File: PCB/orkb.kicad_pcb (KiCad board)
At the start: 2 copper layers, 148.5 x 113.3 mm, 109 parts, among them J1 USB_C_Receptacle_USB2.0, P1 OLED, SW1 MXHS, SW10 MXHS, SW11 MXHS, SW12 MXHS, SW13 MXHS, SW14 MXHS, SW15 MXHS, SW16 MXHS, SW17 MXHS, SW18 MXHS, SW19 MXHS, SW2 MXHS, SW20 MXHS, SW21 MXHS, SW22 MXHS, SW23 MXHS, SW24 MSK12C02, SW25 MSK12C02, SW3 MXHS, SW4 MXHS, SW5 MXHS, SW6 MXHS, SW7 MXHS, SW8 MXHS, SW9 MXHS, U1 ProMicro, U2 SRV05-4, U3 SRV05-4

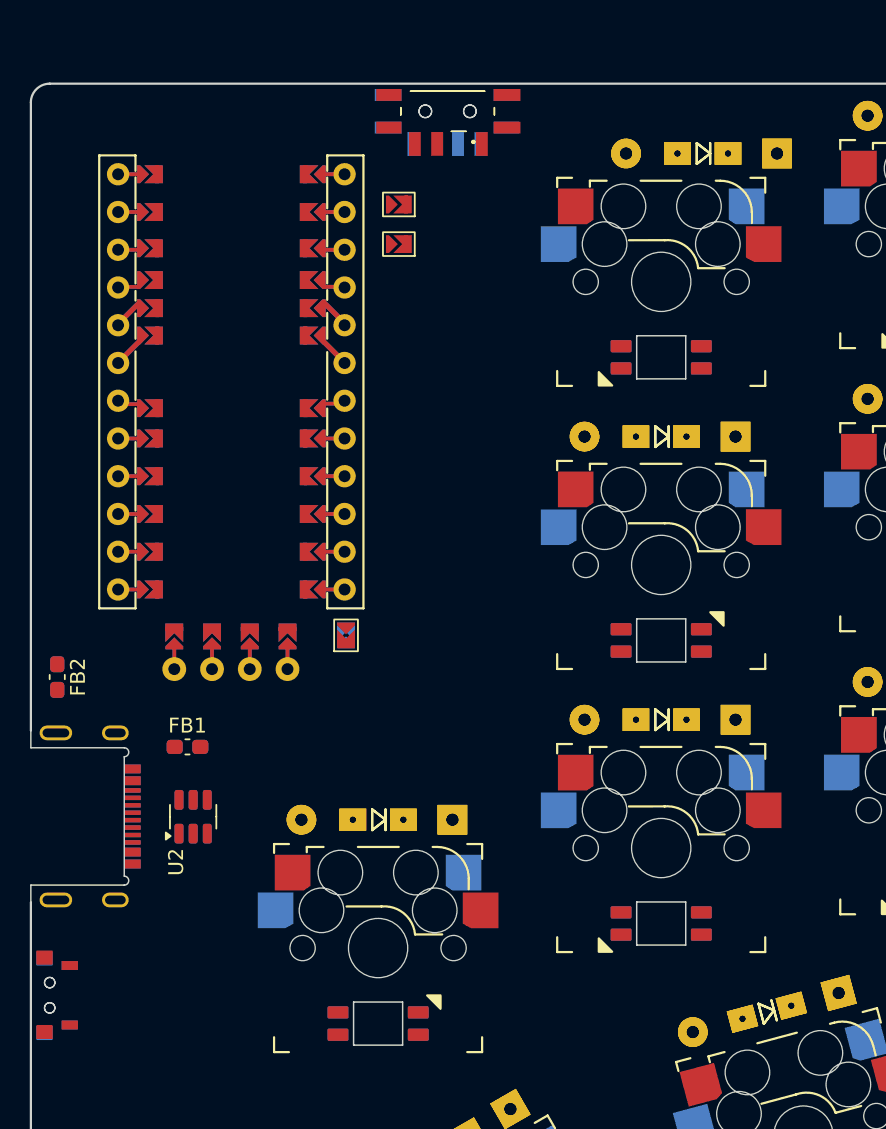
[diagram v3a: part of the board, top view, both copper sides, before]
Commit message: Added underglow LED to schematic
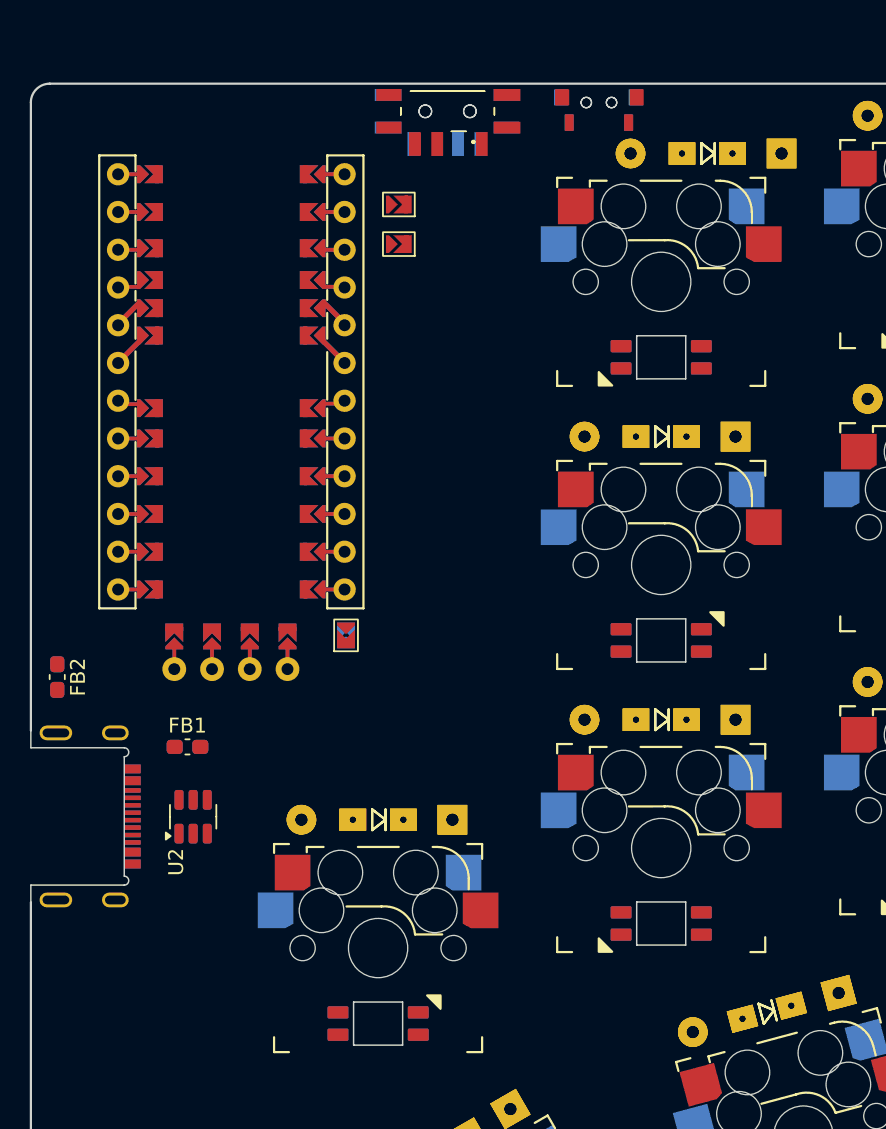
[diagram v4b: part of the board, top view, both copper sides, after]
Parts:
- moved RES1 70.5 mm to (103.5, 48.5), turned to 0 degrees
- moved RES2 70.5 mm to (103.5, 48.5), turned to 180 degrees
- moved D1 0.30 mm to (110.8, 51.9)
- moved D23 0.30 mm to (110.8, 51.9)
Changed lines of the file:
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@@
 		(placed yes)
 		(layer "F.Cu")
-		(at 110.49 51.943 180)
+		(at 110.793 51.943 180)
 		(descr "Diode, DO-41, SOD81, Horizontal, RM 10mm,")
 		(tags "Diode, DO-41, SOD81, Horizontal, RM 10mm, 1N4007, SB140,")
@@
 	(footprint "SplitKeyboard_Common:YTS-A002"
 		(layer "F.Cu")
-		(at 66.548 108.585 90)
+		(at 103.505 48.514)
 		(property "Reference" "RES1"
-			(at 0 -3.2 90)
+			(at 0 -3.2 0)
 			(unlocked yes)
 			(layer "F.SilkS")
@@
 		)
 		(property "Value" "TS-A002_TactileSW"
-			(at -1.269999 -5.08 90)
+			(at -1.269999 -5.080002 0)
 			(unlocked yes)
 			(layer "F.Fab")
@@
 		)
 		(property "Footprint" "SplitKeyboard_Common:YTS-A002"
-			(at 0 0 90)
+			(at 0 0 0)
 			(unlocked yes)
 			(layer "F.Fab")
@@
 		)
 		(property "Datasheet" ""
-			(at 0 0 90)
+			(at 0 0 0)
 			(unlocked yes)
 			(layer "F.Fab")
@@
 		)
 		(property "Description" ""
-			(at 0 0 90)
+			(at 0 0 0)
 			(unlocked yes)
 			(layer "F.Fab")
@@
 		)
 		(property "LCSC" "C2888934"
-			(at 0 0 90)
+			(at 0 0 0)
 			(layer "F.Fab")
 			(hide yes)
@@
 		(fp_poly
 			(pts
-				(xy -0.95 -2.1) (xy 0.95 -2.1) (xy 0.95 -0.9) (xy -0.95 -0.9)
+				(xy -2.4 -0.849996) (xy 2.400002 -0.850001) (xy 2.400001 1.55) (xy -2.399998 1.550001)
 			)
 			(stroke
@@
 		(fp_poly
 			(pts
-				(xy -2.4 -0.849996) (xy 2.400002 -0.850001) (xy 2.400001 1.55) (xy -2.399998 1.550001)
+				(xy -0.95 -2.1) (xy 0.95 -2.1) (xy 0.95 -0.9) (xy -0.95 -0.9)
 			)
 			(stroke
@@
 		)
 		(pad "" np_thru_hole circle
-			(at -0.85 0 90)
+			(at -0.85 0)
 			(size 0.7 0.7)
 			(drill 0.7)
@@
 		)
 		(pad "" np_thru_hole circle
-			(at 0.85 0 90)
+			(at 0.85 0)
 			(size 0.7 0.7)
 			(drill 0.7)
@@
 		)
 		(pad "1" smd roundrect
-			(at -2 1.349999 90)
+			(at -2 1.349999)
 			(size 0.6 1.1)
 			(layers "F.Cu" "F.Paste" "F.Mask")
@@
 		)
 		(pad "2" smd roundrect
-			(at 1.999999 1.350001 90)
+			(at 1.999999 1.350001)
 			(size 0.6 1.1)
 			(layers "F.Cu" "F.Paste" "F.Mask")
@@
 		)
 		(pad "3" smd roundrect
-			(at -2.475 -0.35 90)
+			(at -2.475 -0.35)
 			(size 0.95 1.1)
 			(layers "F.Cu" "F.Paste" "F.Mask")
@@
 		)
 		(pad "3" smd roundrect
-			(at 2.540003 -0.349999 90)
+			(at 2.540003 -0.349999)
 			(size 0.95 1.1)
 			(layers "F.Cu" "F.Paste" "F.Mask")
@@
 		(placed yes)
 		(layer "B.Cu")
-		(at 110.49 51.943 180)
+		(at 110.793 51.943 180)
 		(descr "Diode, DO-41, SOD81, Horizontal, RM 10mm,")
 		(tags "Diode, DO-41, SOD81, Horizontal, RM 10mm, 1N4007, SB140,")
@@
 		(fp_arc
 			(start -1.679999 2.060001)
-			(mid -1.73 2.109999)
+			(mid -1.73 2.109997)
 			(end -1.78 2.06)
 			(stroke
@@
 	(footprint "SplitKeyboard_Common:YTS-A002"
 		(layer "B.Cu")
-		(at 66.548 108.585 -90)
+		(at 103.505 48.514 180)
 		(property "Reference" "RES2"
-			(at 0 3.2 90)
+			(at 0 3.2 0)
 			(unlocked yes)
 			(layer "B.SilkS")
@@
 		)
 		(property "Value" "TS-A002_TactileSW"
-			(at -1.27 5.080001 90)
+			(at -1.269998 5.080001 0)
 			(unlocked yes)
 			(layer "B.Fab")
@@
 		)
 		(property "Footprint" "SplitKeyboard_Common:YTS-A002"
-			(at 0 0 90)
+			(at 0 0 0)
 			(unlocked yes)
 			(layer "B.Fab")
@@
 		)
 		(property "Datasheet" ""
-			(at 0 0 90)
+			(at 0 0 0)
 			(unlocked yes)
 			(layer "B.Fab")
@@
 		)
 		(property "Description" ""
-			(at 0 0 90)
+			(at 0 0 0)
 			(unlocked yes)
 			(layer "B.Fab")
@@
 		)
 		(property "LCSC" "C2888934"
-			(at 0 0 90)
+			(at 0 0 0)
 			(layer "B.Fab")
 			(hide yes)
@@
 		(fp_poly
 			(pts
-				(xy 0.95 0.9) (xy -0.95 0.9) (xy -0.95 2.1) (xy 0.95 2.1)
+				(xy 2.399998 -1.550001) (xy -2.400001 -1.55) (xy -2.400002 0.850001) (xy 2.4 0.849996)
 			)
 			(stroke
@@
 		(fp_poly
 			(pts
-				(xy 2.399998 -1.550001) (xy -2.400001 -1.55) (xy -2.400002 0.850001) (xy 2.4 0.849996)
+				(xy 0.95 0.9) (xy -0.95 0.9) (xy -0.95 2.1) (xy 0.95 2.1)
 			)
 			(stroke
@@
 		)
 		(pad "" np_thru_hole circle
-			(at -0.85 0 270)
+			(at -0.85 0 180)
 			(size 0.7 0.7)
 			(drill 0.7)
@@
 		)
 		(pad "" np_thru_hole circle
-			(at 0.85 0 270)
+			(at 0.85 0 180)
 			(size 0.7 0.7)
 			(drill 0.7)
@@
 		)
 		(pad "1" smd roundrect
-			(at -1.999999 -1.350001 270)
+			(at -1.999999 -1.350001 180)
 			(size 0.6 1.1)
 			(layers "B.Cu" "B.Paste" "B.Mask")
@@
 		)
 		(pad "2" smd roundrect
-			(at 2 -1.349999 270)
+			(at 2 -1.349999 180)
 			(size 0.6 1.1)
 			(layers "B.Cu" "B.Paste" "B.Mask")
@@
 		)
 		(pad "3" smd roundrect
-			(at -2.475 0.35 270)
+			(at -2.475 0.35 180)
 			(size 0.95 1.1)
 			(layers "B.Cu" "B.Paste" "B.Mask")
@@
 		)
 		(pad "3" smd roundrect
-			(at 2.54 0.349999 270)
+			(at 2.54 0.349999 180)
 			(size 0.95 1.1)
 			(layers "B.Cu" "B.Paste" "B.Mask")

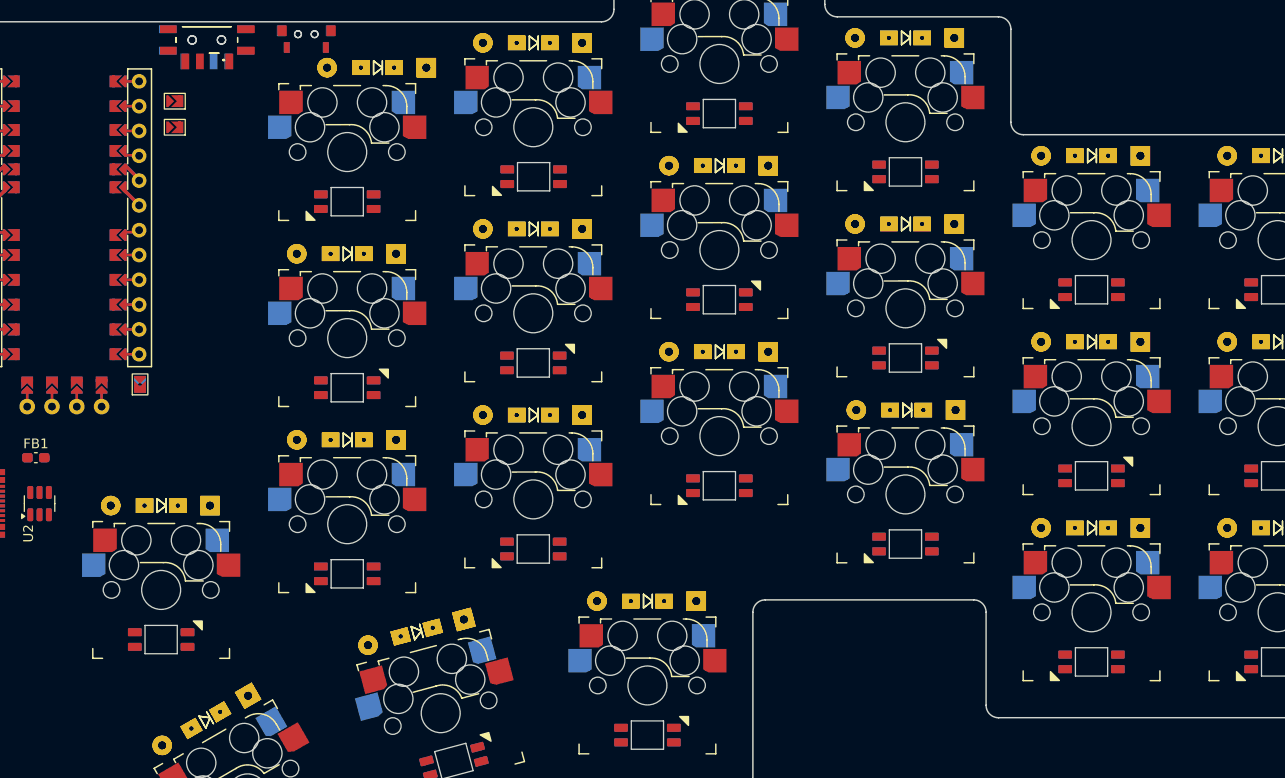
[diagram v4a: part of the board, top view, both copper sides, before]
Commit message: Added underglow LEDs to PCB
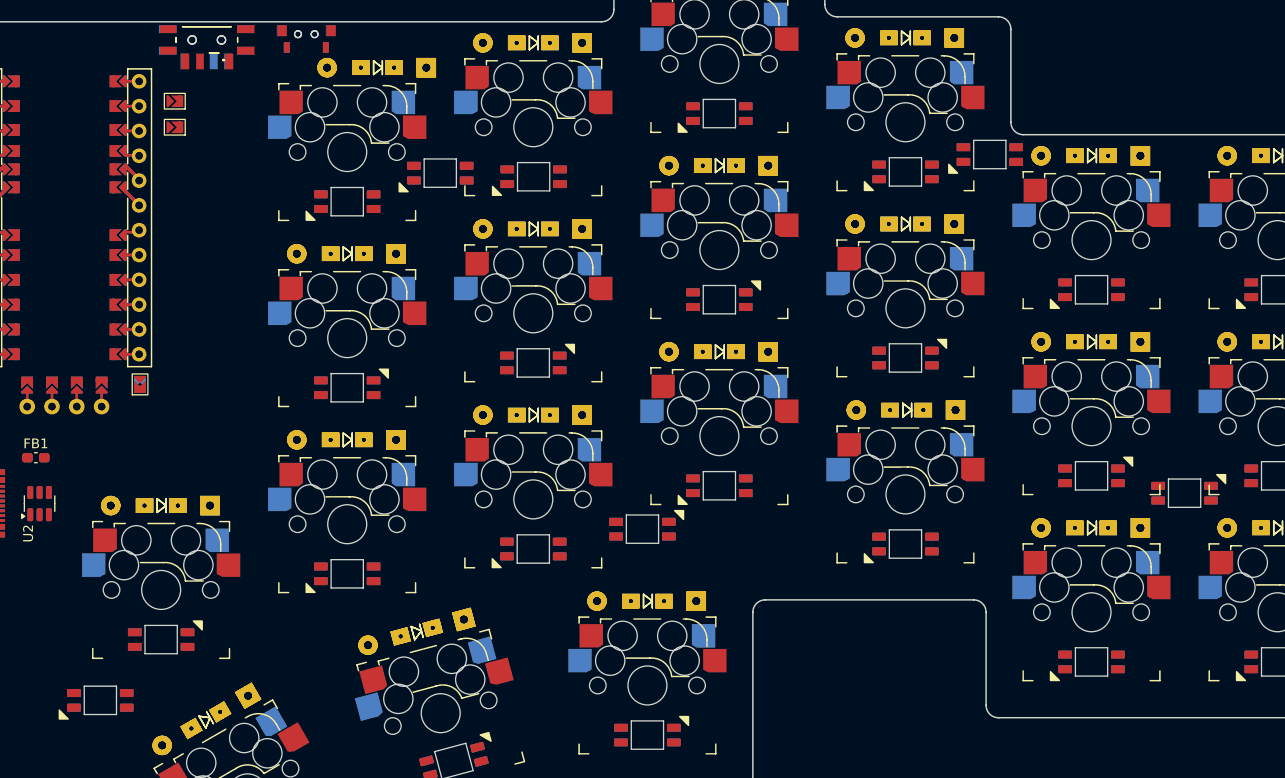
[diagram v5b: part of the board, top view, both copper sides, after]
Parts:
- added LED24: SK6803MINI-E, SplitKeyboard_Common:MX_SK6812MINI-E_REVERSIBLE, B.Cu at (117.2, 62.7)
- added LED25: SK6803MINI-E, SplitKeyboard_Common:MX_SK6812MINI-E_REVERSIBLE, B.Cu at (173.5, 60.8)
- added LED26: SK6803MINI-E, SplitKeyboard_Common:MX_SK6812MINI-E_REVERSIBLE, F.Cu at (193.4, 95.5)
- added LED27: SK6803MINI-E, SplitKeyboard_Common:MX_SK6812MINI-E_REVERSIBLE, F.Cu at (137.9, 99.2)
- added LED28: SK6803MINI-E, SplitKeyboard_Common:MX_SK6812MINI-E_REVERSIBLE, B.Cu at (82.4, 116.7)

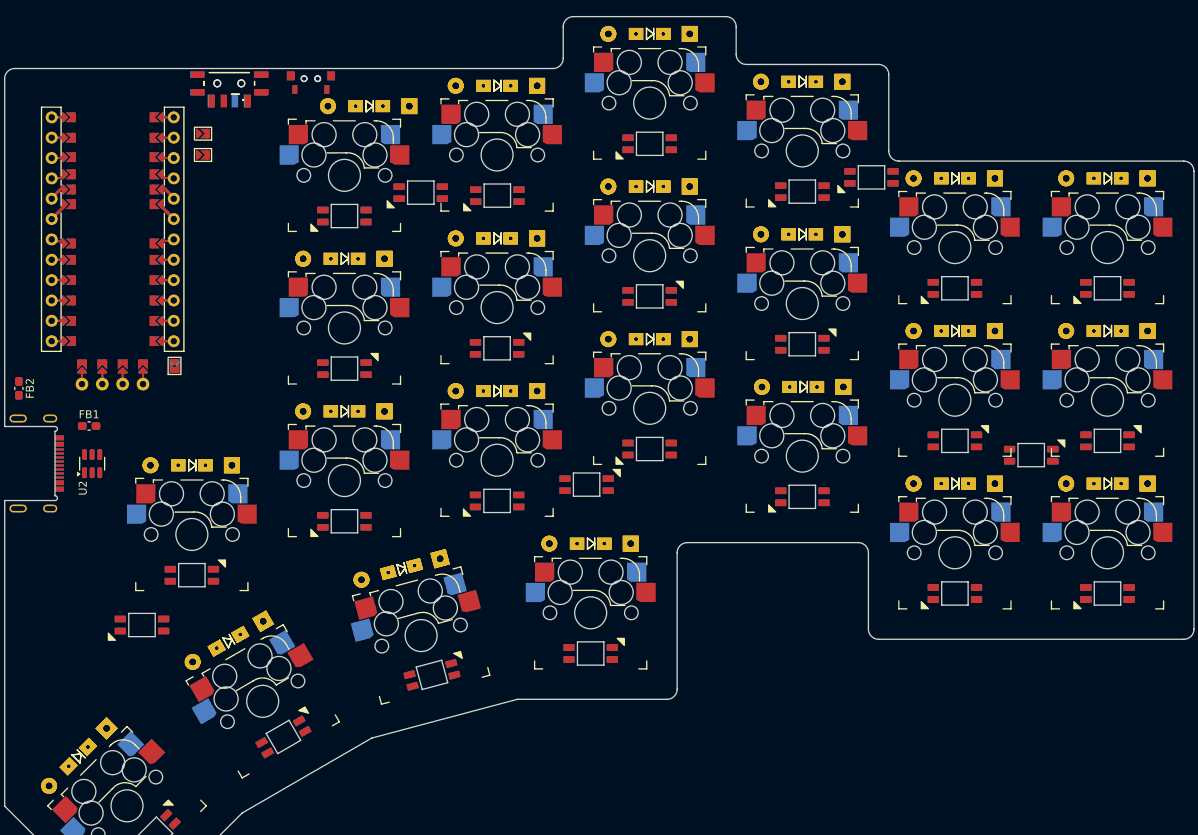
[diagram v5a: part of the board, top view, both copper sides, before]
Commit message: LED double-sided routing for row0
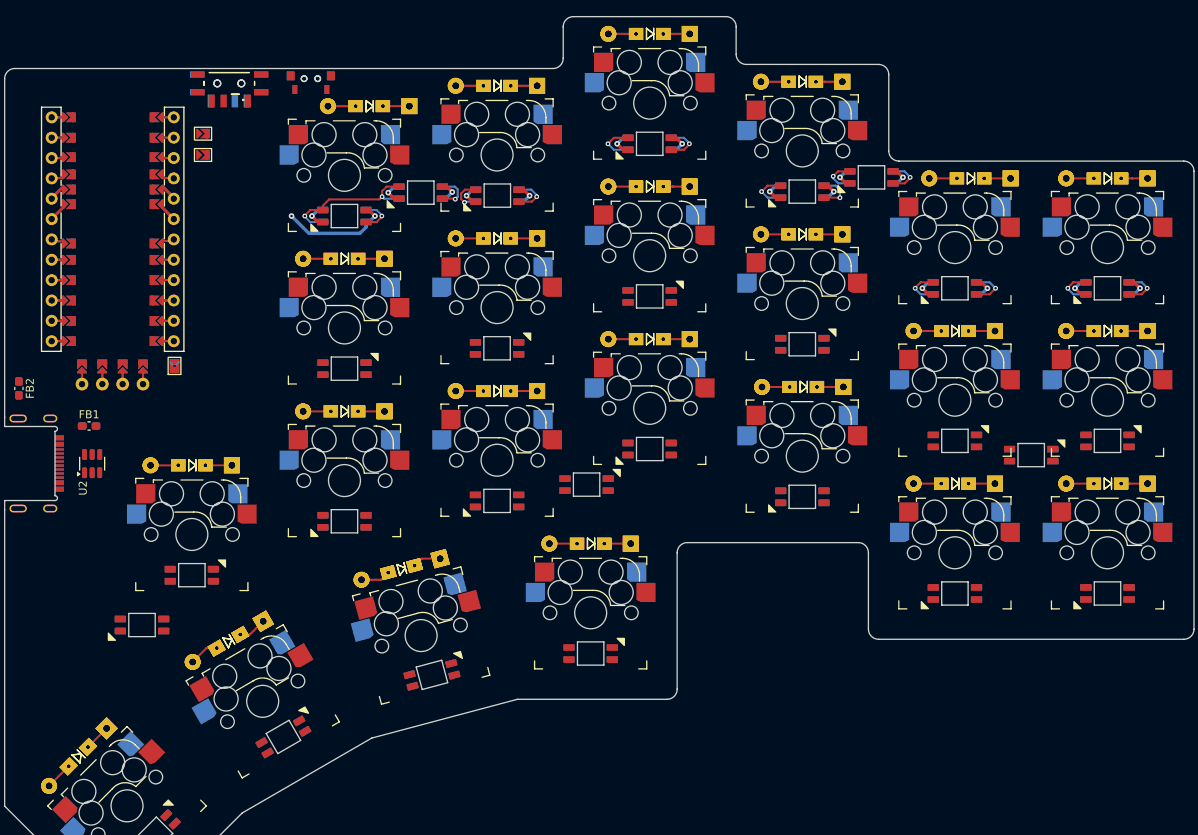
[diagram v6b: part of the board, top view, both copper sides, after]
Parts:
- moved D27 1.95 mm to (185.8, 61.0)
- moved D5 1.95 mm to (185.8, 61.0)
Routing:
- net /PWR_KEY: track 0.00 -> 30.4 mm, vias 0 -> 7
- net GND: track 0.00 -> 26.1 mm, vias 0 -> 8
- net row2: track 0.00 -> 19.8 mm
- net row0: track 0.00 -> 19.8 mm
- net row1: track 0.00 -> 19.8 mm
- net LED: track 0.00 -> 18.9 mm, vias 0 -> 2
- net row3: track 0.00 -> 17.0 mm
- net Net-(LED2-DOUT): track 0.00 -> 10.8 mm, vias 0 -> 2
- net Net-(LED5-DOUT): track 0.00 -> 10.6 mm, vias 0 -> 2
- net Net-(LED3-DOUT): track 0.00 -> 10.6 mm, vias 0 -> 2
- net Net-(LED4-DOUT): track 0.00 -> 10.4 mm, vias 0 -> 2
- net Net-(LED24-DOUT): track 0.00 -> 9.96 mm, vias 0 -> 2
- net Net-(LED1-DOUT): track 0.00 -> 9.43 mm, vias 0 -> 2
- net /PWR_GLOW: track 0.00 -> 6.19 mm, vias 0 -> 2
- net Net-(LED12-DIN): track 0.00 -> 5.20 mm, vias 0 -> 1
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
